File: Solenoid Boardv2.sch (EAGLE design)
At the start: 38 parts, among them Y2 ECS-80-S-4X

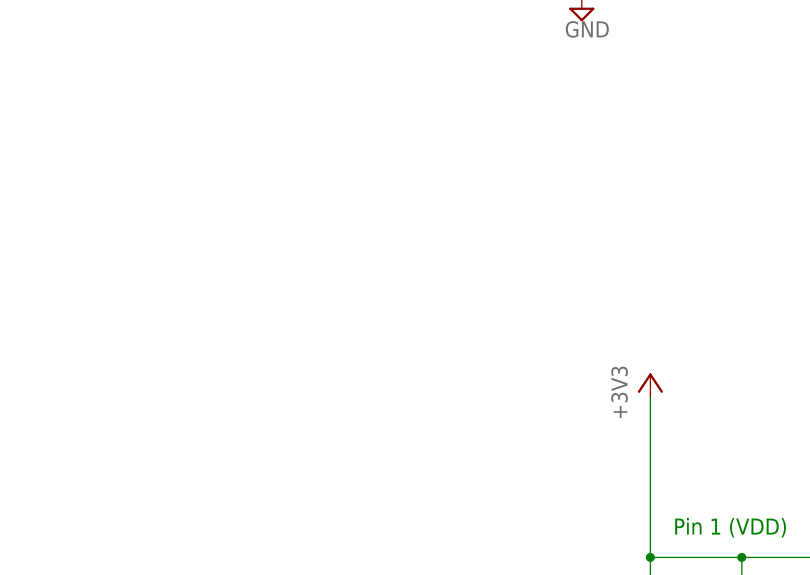
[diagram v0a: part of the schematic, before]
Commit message: Made progress on V2, added polygons and headers for step down converter
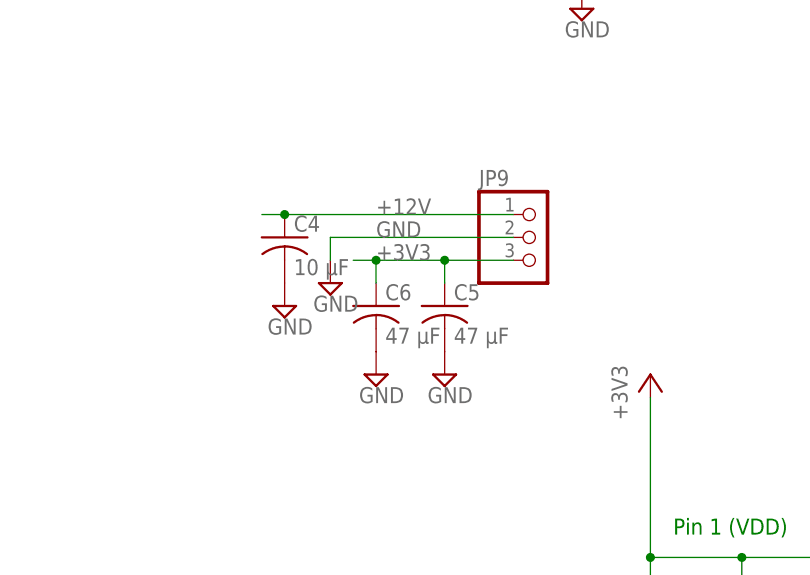
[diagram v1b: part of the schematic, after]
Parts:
- added C4: 10 µF, rcl:C-USC0805
- added C5, C6: 47 µF, rcl:C-USC0805
- added JP9: (no value), pinhead:PINHD-1X3
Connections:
- net +12V: now also C4.1, JP9.1
- net +3V3: now also C5.1, C6.1, JP9.3
- net GND: now also C4.2, C5.2, C6.2, JP9.2
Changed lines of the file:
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@@
 <part name="+3V4" library="supply1" library_urn="urn:adsk.eagle:library:371" deviceset="+3V3" device=""/>
 <part name="R10" library="SparkFun-Resistors" library_urn="urn:adsk.eagle:library:532" deviceset="1KOHM" device="-0603-1/10W-1%" package3d_urn="urn:adsk.eagle:package:39650/1" value="0"/>
+<part name="JP9" library="pinhead" library_urn="urn:adsk.eagle:library:325" deviceset="PINHD-1X3" device="" package3d_urn="urn:adsk.eagle:package:22458/2"/>
+<part name="C4" library="rcl" library_urn="urn:adsk.eagle:library:334" deviceset="C-US" device="C0805" package3d_urn="urn:adsk.eagle:package:23617/2" value="10 µF"/>
+<part name="C5" library="rcl" library_urn="urn:adsk.eagle:library:334" deviceset="C-US" device="C0805" package3d_urn="urn:adsk.eagle:package:23617/2" value="47 µF"/>
+<part name="C6" library="rcl" library_urn="urn:adsk.eagle:library:334" deviceset="C-US" device="C0805" package3d_urn="urn:adsk.eagle:package:23617/2" value="47 µF"/>
+<part name="GND1" library="supply2" library_urn="urn:adsk.eagle:library:372" deviceset="GND" device=""/>
+<part name="GND2" library="supply2" library_urn="urn:adsk.eagle:library:372" deviceset="GND" device=""/>
+<part name="GND3" library="supply2" library_urn="urn:adsk.eagle:library:372" deviceset="GND" device=""/>
+<part name="GND4" library="supply2" library_urn="urn:adsk.eagle:library:372" deviceset="GND" device=""/>
 </parts>
 <sheets>
@@
 <attribute name="NAME" x="475.996" y="132.08" size="1.778" layer="95" font="vector" rot="R90" align="bottom-center"/>
 <attribute name="VALUE" x="479.044" y="132.08" size="1.778" layer="96" font="vector" rot="R90" align="top-center"/>
+</instance>
+<instance part="JP9" gate="A" x="347.98" y="106.68">
+<attribute name="NAME" x="341.63" y="112.395" size="1.778" layer="95"/>
+<attribute name="VALUE" x="341.63" y="99.06" size="1.778" layer="96"/>
+</instance>
+<instance part="C4" gate="G$1" x="320.04" y="106.68">
+<attribute name="NAME" x="321.056" y="107.315" size="1.778" layer="95"/>
+<attribute name="VALUE" x="321.056" y="102.489" size="1.778" layer="96"/>
+</instance>
+<instance part="C5" gate="G$1" x="337.82" y="99.06">
+<attribute name="NAME" x="338.836" y="99.695" size="1.778" layer="95"/>
+<attribute name="VALUE" x="338.836" y="94.869" size="1.778" layer="96"/>
+</instance>
+<instance part="C6" gate="G$1" x="330.2" y="99.06">
+<attribute name="NAME" x="331.216" y="99.695" size="1.778" layer="95"/>
+<attribute name="VALUE" x="331.216" y="94.869" size="1.778" layer="96"/>
+</instance>
+<instance part="GND1" gate="GND" x="320.04" y="99.06">
+<attribute name="VALUE" x="318.135" y="95.885" size="1.778" layer="96"/>
+</instance>
+<instance part="GND2" gate="GND" x="330.2" y="91.44">
+<attribute name="VALUE" x="328.295" y="88.265" size="1.778" layer="96"/>
+</instance>
+<instance part="GND3" gate="GND" x="337.82" y="91.44">
+<attribute name="VALUE" x="335.915" y="88.265" size="1.778" layer="96"/>
+</instance>
+<instance part="GND4" gate="GND" x="325.12" y="101.6">
+<attribute name="VALUE" x="323.215" y="98.425" size="1.778" layer="96"/>
 </instance>
 </instances>
@@
 <junction x="490.22" y="83.82"/>
 </segment>
+<segment>
+<pinref part="JP9" gate="A" pin="2"/>
+<label x="330.2" y="106.68" size="1.778" layer="95"/>
+<wire x1="345.44" y1="106.68" x2="325.12" y2="106.68" width="0.1524" layer="91"/>
+<pinref part="GND4" gate="GND" pin="GND"/>
+<wire x1="325.12" y1="104.14" x2="325.12" y2="106.68" width="0.1524" layer="91"/>
+</segment>
+<segment>
+<pinref part="GND1" gate="GND" pin="GND"/>
+<pinref part="C4" gate="G$1" pin="2"/>
+</segment>
+<segment>
+<pinref part="GND2" gate="GND" pin="GND"/>
+<pinref part="C6" gate="G$1" pin="2"/>
+</segment>
+<segment>
+<pinref part="GND3" gate="GND" pin="GND"/>
+<pinref part="C5" gate="G$1" pin="2"/>
+</segment>
 </net>
 <net name="+12V" class="0">
@@
 <wire x1="66.04" y1="83.82" x2="53.34" y2="83.82" width="0.1524" layer="91"/>
 <wire x1="53.34" y1="83.82" x2="53.34" y2="73.66" width="0.1524" layer="91"/>
+</segment>
+<segment>
+<pinref part="JP9" gate="A" pin="1"/>
+<wire x1="345.44" y1="109.22" x2="320.04" y2="109.22" width="0.1524" layer="91"/>
+<label x="330.2" y="109.22" size="1.778" layer="95"/>
+<pinref part="C4" gate="G$1" pin="1"/>
+<wire x1="320.04" y1="109.22" x2="317.5" y2="109.22" width="0.1524" layer="91"/>
+<junction x="320.04" y="109.22"/>
 </segment>
 </net>
@@
 <label x="391.16" y="147.32" size="1.778" layer="95"/>
 </segment>
-</net>
+<segment>
+<pinref part="JP9" gate="A" pin="3"/>
+<wire x1="345.44" y1="104.14" x2="337.82" y2="104.14" width="0.1524" layer="91"/>
+<label x="330.2" y="104.14" size="1.778" layer="95"/>
+<pinref part="C6" gate="G$1" pin="1"/>
+<wire x1="337.82" y1="104.14" x2="330.2" y2="104.14" width="0.1524" layer="91"/>
+<wire x1="330.2" y1="101.6" x2="330.2" y2="104.14" width="0.1524" layer="91"/>
+<pinref part="C5" gate="G$1" pin="1"/>
+<wire x1="337.82" y1="101.6" x2="337.82" y2="104.14" width="0.1524" layer="91"/>
+<junction x="337.82" y="104.14"/>
+<wire x1="330.2" y1="104.14" x2="327.66" y2="104.14" width="0.1524" layer="91"/>
+<junction x="330.2" y="104.14"/>
+</segment>
+</net>

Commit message: Added the can module
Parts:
- added C10: 4.7nF, SparkFun-Capacitors:0.1UF-0603-25V-(+80/-20%)
- added C9: 100nF, SparkFun-Capacitors:4.7UF0603
- added R6, R7: 60, SparkFun-Resistors:1KOHM-0603-1/10W-1%
- added U$8: TCAN337D, PI_Shield_Library:TCAN337D
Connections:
- new net CAN_STM_RX: U$7.PA11, U$8.TXD
- new net CAN_STM_TX: U$7.PA12, U$8.RXD
- new net N$5: C10.2, R6.1, R7.2
- net +3V3: now also C9.1, U$8.VCC
- net CAN_H: now also R6.2, U$8.CANH
- net CAN_L: now also R7.1, U$8.CANL
- net GND: now also C10.1, C9.2, U$8.GND
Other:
- note added: "CAN TERMINATION"
- note added: "CAN TRANSCEIVER"
- moved on the sheet: C1, C2, C3, CF, I1, JP1, JP2, JP3, JP4, JP5, JP6, JP7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

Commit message: changes from design review
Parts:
- added C7: 47uF, SparkFun-Capacitors:47UF-POLAR-PANASONIC_D-35V-20%
- added H1, H2, H3: STAND-OFF, SparkFun-Hardware:STAND-OFF
- added U$4: 12-TO-3.3-DC-DC, minirov:12-TO-3.3-DC-DC
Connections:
- net +12V: now also C7.+, U$4.VIN
- net +3V3: now also U$4.3.3V
- net GND: now also C7.-, U$4.GND
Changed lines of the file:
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@@
 <?xml version="1.0" encoding="utf-8"?>
 <!DOCTYPE eagle SYSTEM "eagle.dtd">
-<eagle version="9.2.0">
+<eagle version="9.1.3">
 <drawing>
 <settings>
@@
 <layers>
 <layer number="1" name="Top" color="4" fill="1" visible="no" active="no"/>
+<layer number="2" name="Route2" color="16" fill="1" visible="no" active="no"/>
+<layer number="3" name="Route3" color="17" fill="1" visible="no" active="no"/>
+<layer number="4" name="Route4" color="18" fill="1" visible="no" active="no"/>
+<layer number="5" name="Route5" color="19" fill="1" visible="no" active="no"/>
+<layer number="6" name="Route6" color="25" fill="1" visible="no" active="no"/>
+<layer number="7" name="Route7" color="26" fill="1" visible="no" active="no"/>
+<layer number="8" name="Route8" color="27" fill="1" visible="no" active="no"/>
+<layer number="9" name="Route9" color="28" fill="1" visible="no" active="no"/>
+<layer number="10" name="Route10" color="29" fill="1" visible="no" active="no"/>
+<layer number="11" name="Route11" color="30" fill="1" visible="no" active="no"/>
+<layer number="12" name="Route12" color="20" fill="1" visible="no" active="no"/>
+<layer number="13" name="Route13" color="21" fill="1" visible="no" active="no"/>
+<layer number="14" name="Route14" color="22" fill="1" visible="no" active="no"/>
+<layer number="15" name="Route15" color="23" fill="1" visible="no" active="no"/>
 <layer number="16" name="Bottom" color="1" fill="1" visible="no" active="no"/>
 <layer number="17" name="Pads" color="2" fill="1" visible="no" active="no"/>
@@
 <part name="C10" library="SparkFun-Capacitors" library_urn="urn:adsk.eagle:library:510" deviceset="0.1UF" device="-0603-25V-(+80/-20%)" package3d_urn="urn:adsk.eagle:package:37414/1" value="4.7nF"/>
 <part name="GND12" library="supply1" library_urn="urn:adsk.eagle:library:371" deviceset="GND" device=""/>
+<part name="U$4" library="minirov" deviceset="12-TO-3.3-DC-DC" device=""/>
+<part name="GND13" library="supply1" library_urn="urn:adsk.eagle:library:371" deviceset="GND" device=""/>
+<part name="+3V2" library="supply1" library_urn="urn:adsk.eagle:library:371" deviceset="+3V3" device=""/>
+<part name="+12V1" library="supply1" library_urn="urn:adsk.eagle:library:371" deviceset="VCC" device="" value="+12V"/>
+<part name="C7" library="SparkFun-Capacitors" library_urn="urn:adsk.eagle:library:510" deviceset="47UF-POLAR" device="-PANASONIC_D-35V-20%" package3d_urn="urn:adsk.eagle:package:37420/1" value="47uF"/>
+<part name="SUPPLY6" library="supply2" library_urn="urn:adsk.eagle:library:372" deviceset="GND" device=""/>
+<part name="+12V2" library="supply1" library_urn="urn:adsk.eagle:library:371" deviceset="VCC" device="" value="+12V"/>
+<part name="H1" library="SparkFun-Hardware" library_urn="urn:adsk.eagle:library:519" deviceset="STAND-OFF" device="" package3d_urn="urn:adsk.eagle:package:38630/1"/>
+<part name="H2" library="SparkFun-Hardware" library_urn="urn:adsk.eagle:library:519" deviceset="STAND-OFF" device="" package3d_urn="urn:adsk.eagle:package:38630/1"/>
+<part name="H3" library="SparkFun-Hardware" library_urn="urn:adsk.eagle:library:519" deviceset="STAND-OFF" device="" package3d_urn="urn:adsk.eagle:package:38630/1"/>
 </parts>
 <sheets>
@@
 <attribute name="VALUE" x="175.26" y="137.16" size="1.778" layer="96"/>
 </instance>
+<instance part="U$4" gate="A" x="220.98" y="101.6"/>
+<instance part="GND13" gate="1" x="220.98" y="88.9">
+<attribute name="VALUE" x="218.44" y="86.36" size="1.778" layer="96"/>
+</instance>
+<instance part="+3V2" gate="G$1" x="238.76" y="114.3">
+<attribute name="VALUE" x="236.22" y="109.22" size="1.778" layer="96" rot="R90"/>
+</instance>
+<instance part="+12V1" gate="VCC" x="203.2" y="114.3">
+<attribute name="VALUE" x="200.66" y="117.475" size="1.778" layer="96"/>
+</instance>
+<instance part="C7" gate="G$1" x="17.78" y="86.36"/>
+<instance part="SUPPLY6" gate="GND" x="17.78" y="76.2">
+<attribute name="VALUE" x="15.875" y="73.025" size="1.778" layer="96"/>
+</instance>
+<instance part="+12V2" gate="VCC" x="17.78" y="93.98">
+<attribute name="VALUE" x="15.24" y="97.155" size="1.778" layer="96"/>
+</instance>
+<instance part="H1" gate="G$1" x="10.16" y="200.66"/>
+<instance part="H2" gate="G$1" x="10.16" y="198.12"/>
+<instance part="H3" gate="G$1" x="12.7" y="200.66"/>
 </instances>
 <busses>
@@
 <wire x1="177.8" y1="142.24" x2="177.8" y2="154.94" width="0.1524" layer="91"/>
 </segment>
+<segment>
+<pinref part="U$4" gate="A" pin="GND"/>
+<wire x1="220.98" y1="93.98" x2="220.98" y2="91.44" width="0.1524" layer="91"/>
+<pinref part="GND13" gate="1" pin="GND"/>
+</segment>
+<segment>
+<pinref part="C7" gate="G$1" pin="-"/>
+<pinref part="SUPPLY6" gate="GND" pin="GND"/>
+<wire x1="17.78" y1="81.28" x2="17.78" y2="78.74" width="0.1524" layer="91"/>
+</segment>
 </net>
 <net name="+12V" class="0">
@@
 <wire x1="35.56" y1="48.26" x2="22.86" y2="48.26" width="0.1524" layer="91"/>
 <wire x1="22.86" y1="48.26" x2="22.86" y2="38.1" width="0.1524" layer="91"/>
+<label x="30.48" y="38.1" size="1.778" layer="95"/>
 </segment>
 <segment>
@@
 <wire x1="320.04" y1="109.22" x2="317.5" y2="109.22" width="0.1524" layer="91"/>
 <junction x="320.04" y="109.22"/>
+</segment>
+<segment>
+<pinref part="U$4" gate="A" pin="VIN"/>
+<wire x1="208.28" y1="106.68" x2="203.2" y2="106.68" width="0.1524" layer="91"/>
+<wire x1="203.2" y1="106.68" x2="203.2" y2="111.76" width="0.1524" layer="91"/>
+<pinref part="+12V1" gate="VCC" pin="VCC"/>
+<label x="200.66" y="104.14" size="1.778" layer="95"/>
+</segment>
+<segment>
+<pinref part="+12V2" gate="VCC" pin="VCC"/>
+<pinref part="C7" gate="G$1" pin="+"/>
+<wire x1="17.78" y1="91.44" x2="17.78" y2="88.9" width="0.1524" layer="91"/>
+<label x="17.78" y="91.44" size="1.778" layer="95"/>
 </segment>
 </net>
@@
 <junction x="68.58" y="175.26"/>
 </segment>
-</net>
+<segment>
+<pinref part="U$4" gate="A" pin="3.3V"/>
+<wire x1="233.68" y1="106.68" x2="238.76" y2="106.68" width="0.1524" layer="91"/>
+<wire x1="238.76" y1="106.68" x2="238.76" y2="111.76" width="0.1524" layer="91"/>
+<pinref part="+3V2" gate="G$1" pin="+3V3"/>
+</segment>
+</net>
